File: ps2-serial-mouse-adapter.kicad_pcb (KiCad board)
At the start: 2 copper layers, 59.1 x 31.7 mm, 10 parts, among them U1 Arduino_Mini, U2 MAX232

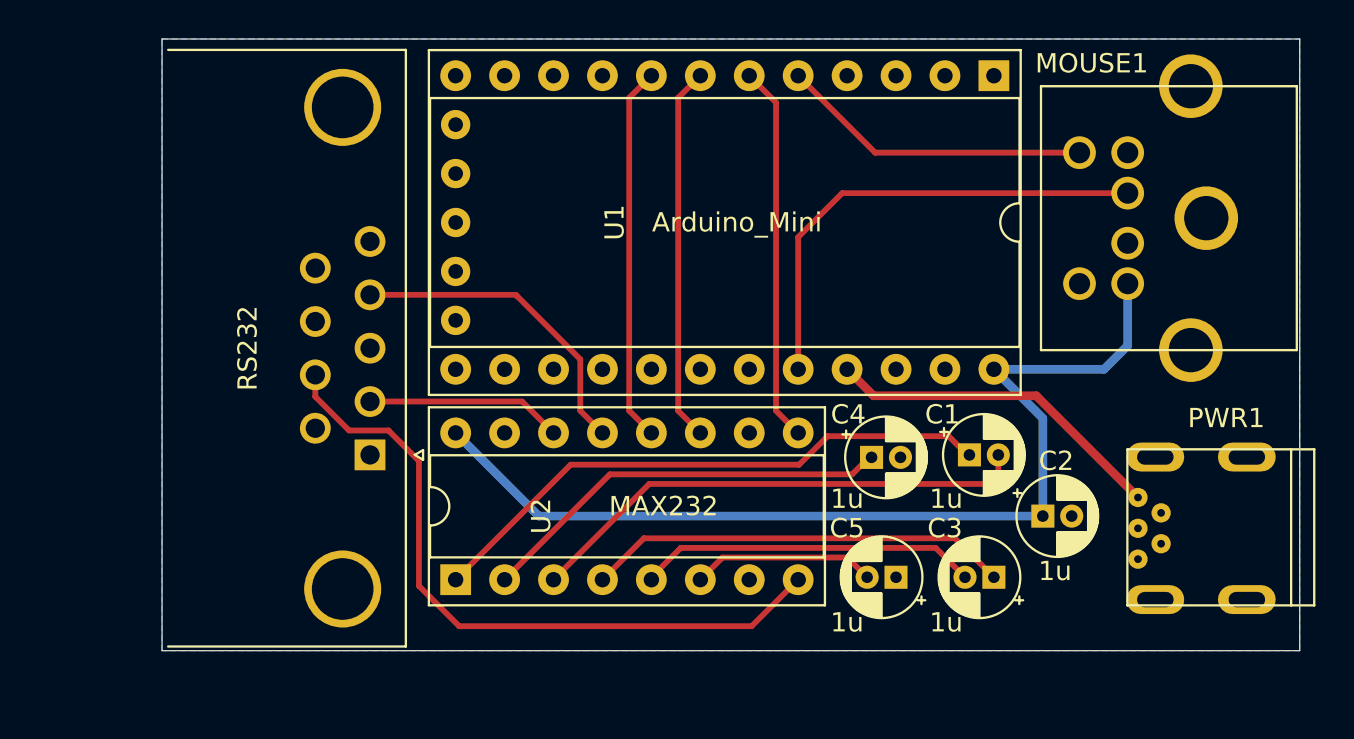
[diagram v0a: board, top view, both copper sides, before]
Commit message: Move MAX232 under the Arduino to save space
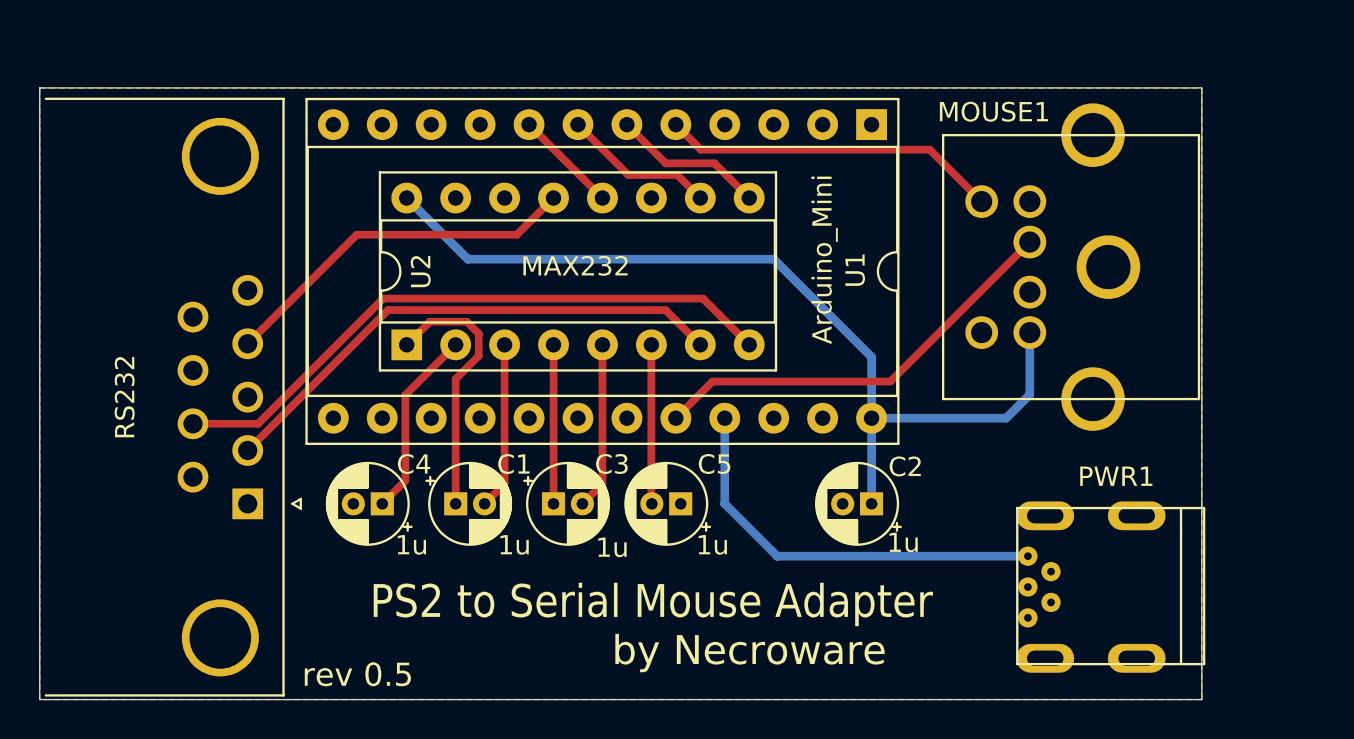
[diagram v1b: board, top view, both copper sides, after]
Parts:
- U1: footprint MyLibrary:Arduino_Mini -> Package_DIP:DIP-24_W15.24mm_Socket
- moved C1 26.8 mm to (102.9, 76.2)
- moved C4 25.5 mm to (99.1, 76.2), turned to 180 degrees
- moved C3 23.2 mm to (108.0, 76.2), turned to 0 degrees
- moved U2 12.5 mm to (100.3, 67.9)
- moved C5 11.8 mm to (114.6, 76.2)
- moved C2 8.91 mm to (124.5, 76.2), turned to 180 degrees
- moved U1 6.84 mm to (124.5, 56.5)
- moved RS232 6.84 mm to (92.1, 76.2)
- moved PWR1 6.48 mm to (136.5, 80.5)
- moved MOUSE1 5.68 mm to (130.2, 67.3)
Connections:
- U2 pad 10: (no net) -> TX
- U2 pad 11: TX -> (no net)
- U2 pad 14: Net-(RS232-Pad2) -> (no net)
- U2 pad 7: (no net) -> Net-(RS232-Pad2)
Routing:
- net Net-(C1-Pad2): track 26.3 -> 8.69 mm
- net Net-(RS232-Pad2): track 10.2 -> 27.3 mm
- net Net-(C1-Pad1): track 30.1 -> 13.8 mm
- net DTS: track 19.5 -> 5.39 mm
- net Net-(C3-Pad1): track 22.0 -> 8.44 mm
- net Net-(C4-Pad1): track 21.6 -> 9.83 mm
- net RTS: track 19.6 -> 7.93 mm
- net TX: track 19.5 -> 7.93 mm
- net Net-(C3-Pad2): track 17.7 -> 8.69 mm
- net Net-(C2-Pad1): track 51.6 -> 47.1 mm
- net VCC: track 17.9 -> 21.3 mm
- net Net-(RS232-Pad7): track 35.9 -> 32.6 mm
- net DATA: track 24.9 -> 22.2 mm
- net Net-(RS232-Pad4): track 16.6 -> 19.0 mm
- net Net-(C5-Pad2): track 9.56 -> 8.26 mm
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- added copper zone on F.Cu, net GND
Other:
- board size 59.1 x 31.7 mm -> 60.3 x 31.8 mm
- net class Default: trace_width 0.3 -> 0.4
- board text added: "PS2 to Serial Mouse Adapter"
- board text added: "by Necroware"
- board text added: "rev 0.5"

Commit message: Add jumpers, fix pwr1
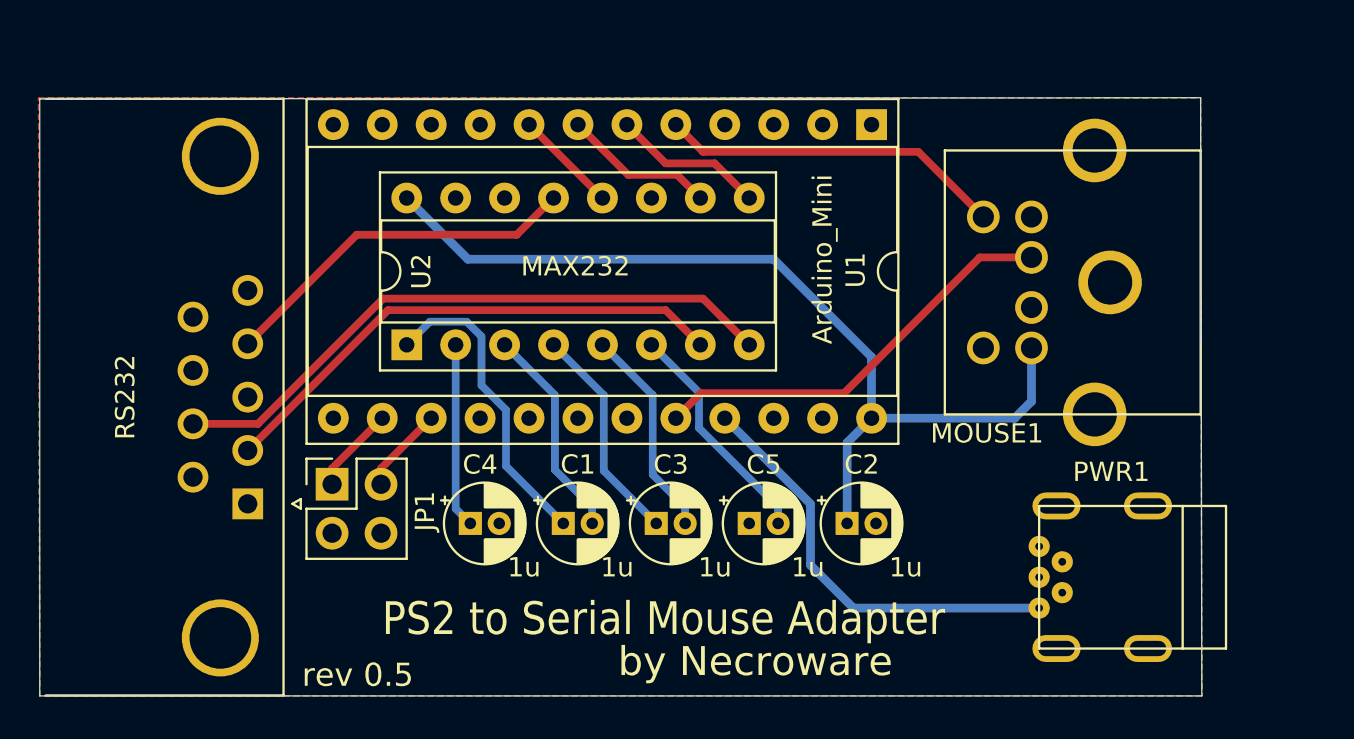
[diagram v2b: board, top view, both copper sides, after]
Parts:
- added JP1: Conn_02x02_Odd_Even, Connector_PinSocket_2.54mm:PinSocket_2x02_P2.54mm_Vertical, F.Cu at (96.5, 75.2)
- moved C1 5.68 mm to (108.5, 77.2)
- moved C3 5.43 mm to (113.3, 77.2)
- moved C4 4.68 mm to (103.6, 77.2), turned to 0 degrees
- moved C5 3.70 mm to (118.1, 77.2), turned to 0 degrees
- moved PWR1 3.40 mm to (133.2, 80.0), turned to 90 degrees
- moved C2 1.63 mm to (123.2, 77.2), turned to 0 degrees
- moved MOUSE1 0.80 mm to (130.3, 68.1)
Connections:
- U1 pad 14: (no net) -> Net-(JP1-Pad1)
- U1 pad 15: (no net) -> Net-(JP1-Pad3)
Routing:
- net Net-(JP1-Pad3): track 0.00 -> 4.51 mm
- net Net-(JP1-Pad1): track 0.00 -> 4.51 mm
- net Net-(C5-Pad2): track 8.26 -> 12.0 mm
- net Net-(C3-Pad1): track 8.44 -> 11.5 mm
- net Net-(C1-Pad2): track 8.69 -> 11.2 mm
- net Net-(C1-Pad1): track 13.8 -> 16.3 mm
- net Net-(C3-Pad2): track 8.69 -> 11.0 mm
- net Net-(C2-Pad1): track 47.1 -> 48.2 mm
- net VCC: track 21.3 -> 22.3 mm
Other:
- board size 60.3 x 31.8 mm -> 60.3 x 31.1 mm
